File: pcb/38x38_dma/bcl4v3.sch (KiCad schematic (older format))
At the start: 23 parts, among them J1 Conn_01x04, J10 Conn_01x04, J2 Conn_01x04, J3 Conn_01x04, J4 Conn_01x04, J5 Conn_01x04, J6 Conn_01x04, J7 Conn_01x04, J8 Conn_01x04, J9 USB_MICRO-B_FEMALE-SMT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

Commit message: Board update
fully routed PCB
indicator LED added
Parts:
- removed R2: 0R, Resistor_SMD:R_0805_2012Metric_Pad1.15x1.40mm_HandSolder, symbol Device:R_Small
- added D1: LED, LED_SMD:LED_0805_2012Metric_Castellated, symbol Device:LED
- added Q1: IRLML6402, Package_TO_SOT_SMD:SOT-23, symbol Transistor_FET:IRLML6402
- added R3: 220R, Resistor_SMD:R_0805_2012Metric_Pad1.15x1.40mm_HandSolder, symbol Device:R_Small
- added R4: R, Resistor_SMD:R_0805_2012Metric_Pad1.15x1.40mm_HandSolder, symbol Device:R
- C1, C2: footprint Capacitor_SMD:C_0805_2012Metric_Pad1.15x1.40mm_HandSolder -> Capacitor_SMD:C_0603_1608Metric_Pad1.05x0.95mm_HandSolder
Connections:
- net labels added: LED, OSC_IN, OSC_OUT
- wire segments 186 -> 192
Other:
- moved on the sheet: C1, C2, C3, C4, J10, U5, Y1

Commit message: PCB and schematics updates
- exchange STM32F070 with STM32F072 (USB w/o HSE)
- remove xtal and related components
- add boot mode jumper pads (NO)
- connect USB_VBUS with VCC via jumper (NC)
- smaller clearance for pad to solder mask
- add local library directory for externally imported
  symbols, footprints and 3D models

PCB outline
add small cut-out for USB receptacle
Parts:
- removed C1, C2: 20pF, Capacitor_SMD:C_0603_1608Metric_Pad1.05x0.95mm_HandSolder, symbol Device:C_Small
- removed J9: USB_MICRO-B_FEMALE-SMT, Connectors:USB-B-MICRO-SMD, symbol SparkFun-Connectors:USB_MICRO-B_FEMALE-SMT
- removed R3: 220R, Resistor_SMD:R_0805_2012Metric_Pad1.15x1.40mm_HandSolder, symbol Device:R_Small
- removed U1: STM32F070CBTx, Package_QFP:LQFP-48_7x7mm_P0.5mm, symbol MCU_ST_STM32F0:STM32F070CBTx
- removed Y1: 8Mhz, Crystal:Crystal_SMD_Abracon_ABM7-2Pin_6.0x3.5mm, symbol Device:Crystal
- added BOOT0: Jumper_2_Open, Jumpers:SMT-JUMPER_2_NO_SILK, symbol Jumper:Jumper_2_Open
- added C5, C6, C7, C8: C_Small, Capacitor_SMD:C_0805_2012Metric_Pad1.15x1.40mm_HandSolder, symbol Device:C_Small
- added J9: 10118194-0001LF, digikey-footprints:USB_Micro_B_Female_10118194-0001LF, symbol dk_USB-DVI-HDMI-Connectors:10118194-0001LF
- added JP1: Jumper, Jumpers:SMT-JUMPER_2_NC_TRACE_NO-SILK, symbol Device:Jumper
- added R2: 1k, Resistor_SMD:R_0805_2012Metric_Pad1.15x1.40mm_HandSolder, symbol Device:R_Small
- added U1: STM32F072CBTx, Package_QFP:LQFP-48_7x7mm_P0.5mm, symbol MCU_ST_STM32F0:STM32F072CBTx
- C3, C4: value C_Small -> 4.7u
- DS1: value TC15-11SRWA -> LDM-1588BS
- J10: footprint Connector_PinHeader_2.54mm:PinHeader_1x04_P2.54mm_Horizontal -> Connector_PinHeader_2.54mm:PinHeader_1x04_P2.54mm_Vertical
- R1: value R -> 1k
- R4: value R -> 680R
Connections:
- net labels added: BOOT0
- net labels removed: OSC_IN, OSC_OUT
- wire segments 192 -> 195
- no-connect marks 2 -> 19
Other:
- moved on the sheet: C3, C4, D1, DS1, J1, J10, J2, J3, J4, J5, J6, J7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

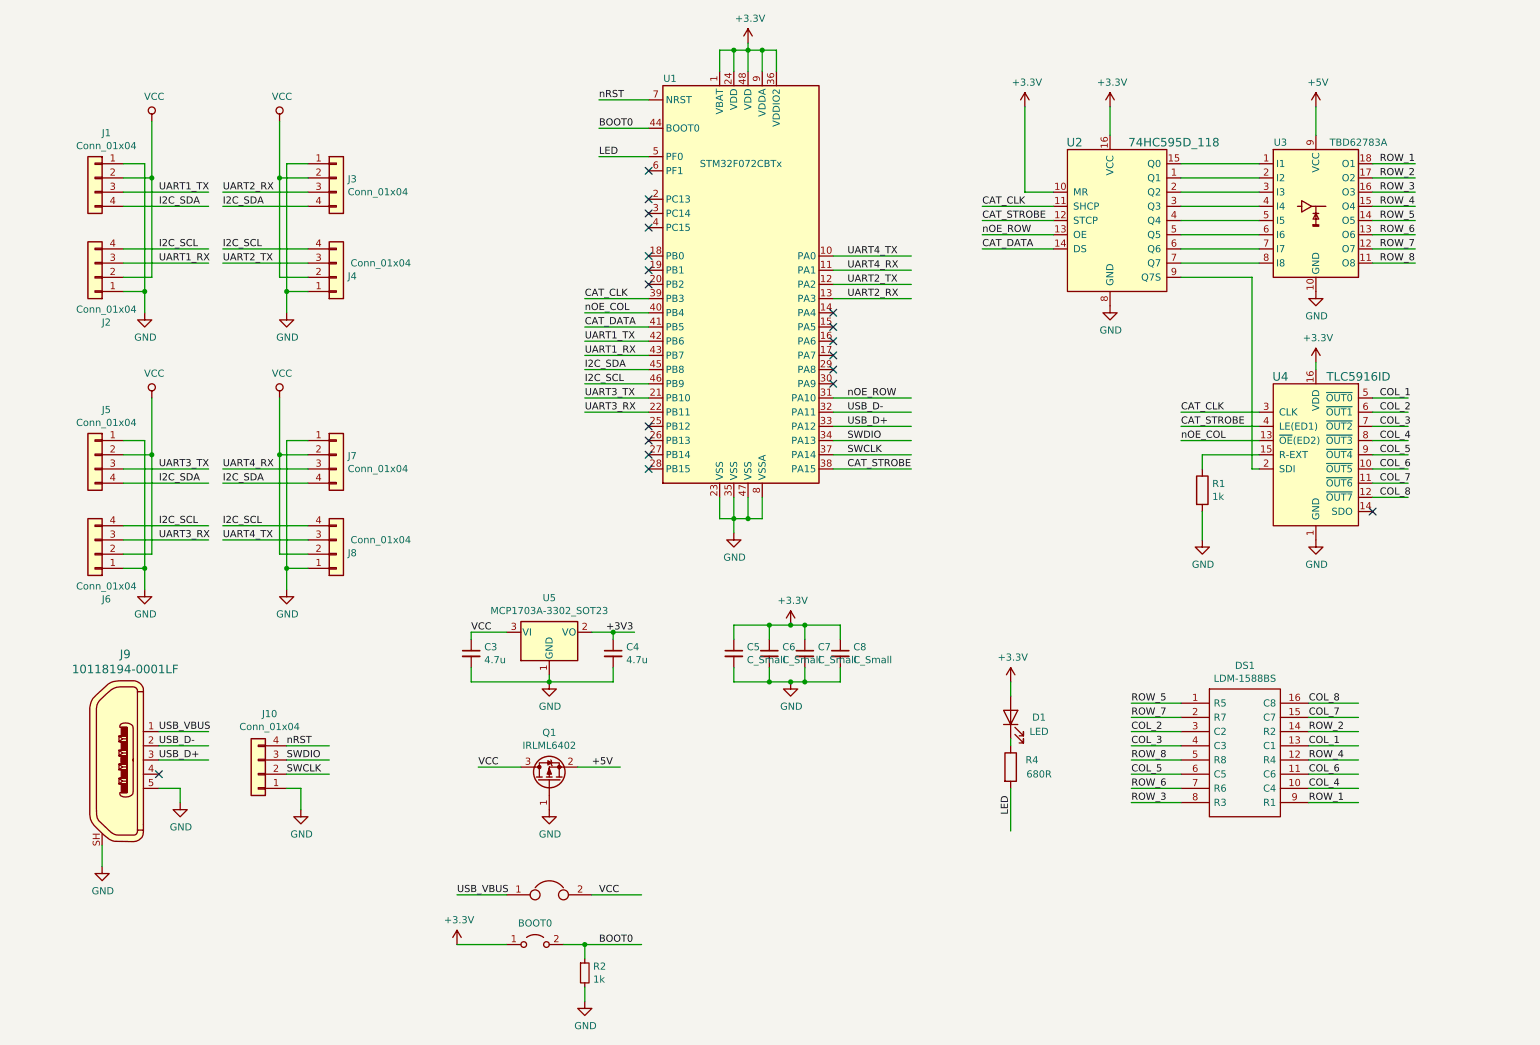
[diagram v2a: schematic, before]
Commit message: PCB and schematics cleanup
resize PCB to exactly 38x38mm, center the LED matrix
add OSHW logo to silk screen, add copyright information
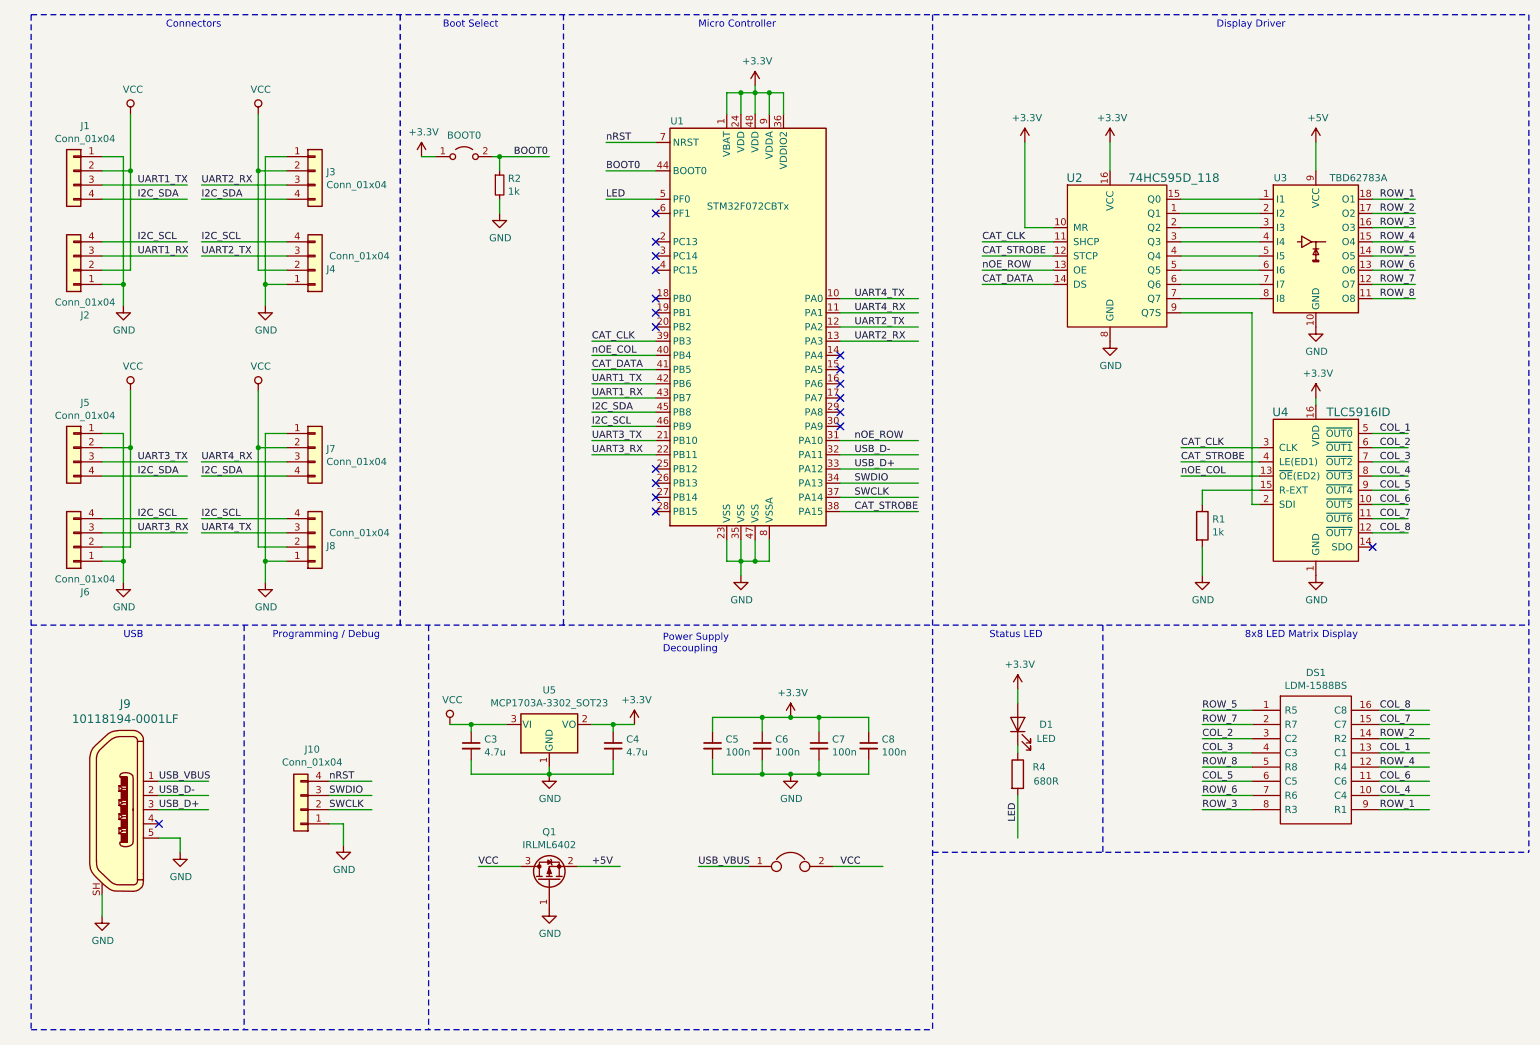
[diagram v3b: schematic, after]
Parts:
- C5, C6, C7, C8: value C_Small -> 100n
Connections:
- net labels removed: +3V3
- wire segments 195 -> 196
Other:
- note added: "8x8 LED Matrix Display"
- note added: "Boot Select"
- note added: "Connectors"
- note added: "Display Driver"
- note added: "Micro Controller"
- note added: "Power Supply\nDecoupling"
- note added: "Programming / Debug"
- note added: "Status LED"
- note added: "USB"
- moved on the sheet: BOOT0, C3, C4, C5, C6, C7, C8, D1, DS1, J1, J10, J2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

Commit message: Fix reverse voltage protection, cleanups
- power from USB doesn't need to go through protection FET
- power to 3.3V LDO _must_ got through protection FET
- add OSHW logo also to schematics so that it doesn't vanish if you
  sync PCB and schematics
- modify copyright info a bit
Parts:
- added LOGO1: OSHW-LOGOM, OSHW-LOGO-M, symbol SparkFun-Aesthetics:OSHW-LOGOM
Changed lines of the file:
@@
 	1050 4250 1650 4250
-$Comp
-L power:VCC #PWR0117
-U 1 1 5BF09410
-P 1250 1300
-F 0 "#PWR0117" H 1250 1150 50  0001 C CNN
-F 1 "VCC" H 1267 1473 50  0000 C CNN
-F 2 "" H 1250 1300 50  0001 C CNN
-F 3 "" H 1250 1300 50  0001 C CNN
-	1    1250 1300
-	1    0    0    -1
-$EndComp
-$Comp
-L power:VCC #PWR0118
-U 1 1 5BF09465
-P 2150 1300
-F 0 "#PWR0118" H 2150 1150 50  0001 C CNN
-F 1 "VCC" H 2167 1473 50  0000 C CNN
-F 2 "" H 2150 1300 50  0001 C CNN
-F 3 "" H 2150 1300 50  0001 C CNN
-	1    2150 1300
-	1    0    0    -1
-$EndComp
-$Comp
-L power:VCC #PWR0119
-U 1 1 5BF094BA
-P 1250 3250
-F 0 "#PWR0119" H 1250 3100 50  0001 C CNN
-F 1 "VCC" H 1267 3423 50  0000 C CNN
-F 2 "" H 1250 3250 50  0001 C CNN
-F 3 "" H 1250 3250 50  0001 C CNN
-	1    1250 3250
-	1    0    0    -1
-$EndComp
-$Comp
-L power:VCC #PWR0120
-U 1 1 5BF0950F
-P 2150 3250
-F 0 "#PWR0120" H 2150 3100 50  0001 C CNN
-F 1 "VCC" H 2167 3423 50  0000 C CNN
-F 2 "" H 2150 3250 50  0001 C CNN
-F 3 "" H 2150 3250 50  0001 C CNN
-	1    2150 3250
-	1    0    0    -1
-$EndComp
 $Comp
 L Regulator_Linear:MCP1703A-3302_SOT23 U5
@@
 USB_VBUS
 Text Label 6250 6600 0    50   ~ 0
-VCC
++5V
 $Comp
 L Device:C_Small C5
@@
 NoConn ~ 4950 4100
 $Comp
-L power:+3.3V #PWR?
+L power:+3.3V #PWR0128
 U 1 1 5BF60507
 P 4800 5600
-F 0 "#PWR?" H 4800 5450 50  0001 C CNN
+F 0 "#PWR0128" H 4800 5450 50  0001 C CNN
 F 1 "+3.3V" H 4815 5773 50  0000 C CNN
 F 2 "" H 4800 5600 50  0001 C CNN
 F 3 "" H 4800 5600 50  0001 C CNN
 	1    4800 5600
-	1    0    0    -1
-$EndComp
-$Comp
-L power:VCC #PWR?
-U 1 1 5BF60582
-P 3500 5600
-F 0 "#PWR?" H 3500 5450 50  0001 C CNN
-F 1 "VCC" H 3517 5773 50  0000 C CNN
-F 2 "" H 3500 5600 50  0001 C CNN
-F 3 "" H 3500 5600 50  0001 C CNN
-	1    3500 5600
 	1    0    0    -1
 $EndComp
@@
 Text Notes 2250 5000 0    50   ~ 0
 Programming / Debug
+$Comp
+L power:+5V #PWR0129
+U 1 1 5BFEB2FC
+P 3500 5600
+F 0 "#PWR0129" H 3500 5450 50  0001 C CNN
+F 1 "+5V" H 3515 5773 50  0000 C CNN
+F 2 "" H 3500 5600 50  0001 C CNN
+F 3 "" H 3500 5600 50  0001 C CNN
+	1    3500 5600
+	1    0    0    -1
+$EndComp
+$Comp
+L power:VCC #PWR0119
+U 1 1 5BF094BA
+P 1250 3250
+F 0 "#PWR0119" H 1250 3100 50  0001 C CNN
+F 1 "VCC" H 1267 3423 50  0000 C CNN
+F 2 "" H 1250 3250 50  0001 C CNN
+F 3 "" H 1250 3250 50  0001 C CNN
+	1    1250 3250
+	1    0    0    -1
+$EndComp
+$Comp
+L power:VCC #PWR0120
+U 1 1 5BF0950F
+P 2150 3250
+F 0 "#PWR0120" H 2150 3100 50  0001 C CNN
+F 1 "VCC" H 2167 3423 50  0000 C CNN
+F 2 "" H 2150 3250 50  0001 C CNN
+F 3 "" H 2150 3250 50  0001 C CNN
+	1    2150 3250
+	1    0    0    -1
+$EndComp
+$Comp
+L power:VCC #PWR0118
+U 1 1 5BF09465
+P 2150 1300
+F 0 "#PWR0118" H 2150 1150 50  0001 C CNN
+F 1 "VCC" H 2167 1473 50  0000 C CNN
+F 2 "" H 2150 1300 50  0001 C CNN
+F 3 "" H 2150 1300 50  0001 C CNN
+	1    2150 1300
+	1    0    0    -1
+$EndComp
+$Comp
+L power:VCC #PWR0117
+U 1 1 5BF09410
+P 1250 1300
+F 0 "#PWR0117" H 1250 1150 50  0001 C CNN
+F 1 "VCC" H 1267 1473 50  0000 C CNN
+F 2 "" H 1250 1300 50  0001 C CNN
+F 3 "" H 1250 1300 50  0001 C CNN
+	1    1250 1300
+	1    0    0    -1
+$EndComp
+$Comp
+L SparkFun-Aesthetics:OSHW-LOGOM LOGO1
+U 1 1 5BFECBD9
+P 3750 4450
+F 0 "LOGO1" H 3750 4700 45  0001 C CNN
+F 1 "OSHW-LOGOM" H 3750 4050 45  0001 C CNN
+F 2 "OSHW-LOGO-M" H 3750 4750 20  0001 C CNN
+F 3 "" H 3750 4450 50  0001 C CNN
+F 4 "XXX-00000" H 4228 4385 60  0001 L CNN "Field4"
+	1    3750 4450
+	1    0    0    -1
+$EndComp
 $EndSCHEMATC

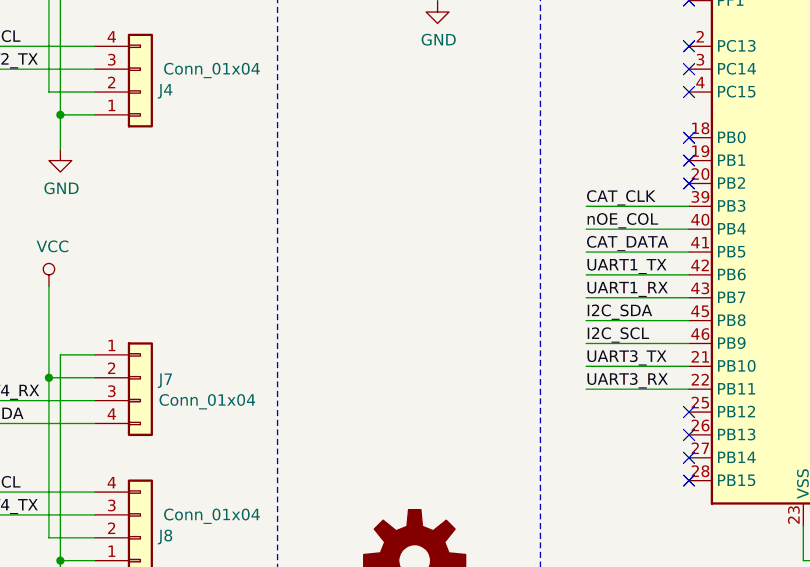
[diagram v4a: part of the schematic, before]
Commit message: Add test points, small routing changes
- add test points for SPI bus
- add net classes for VCC and LED networks
- small routing changes
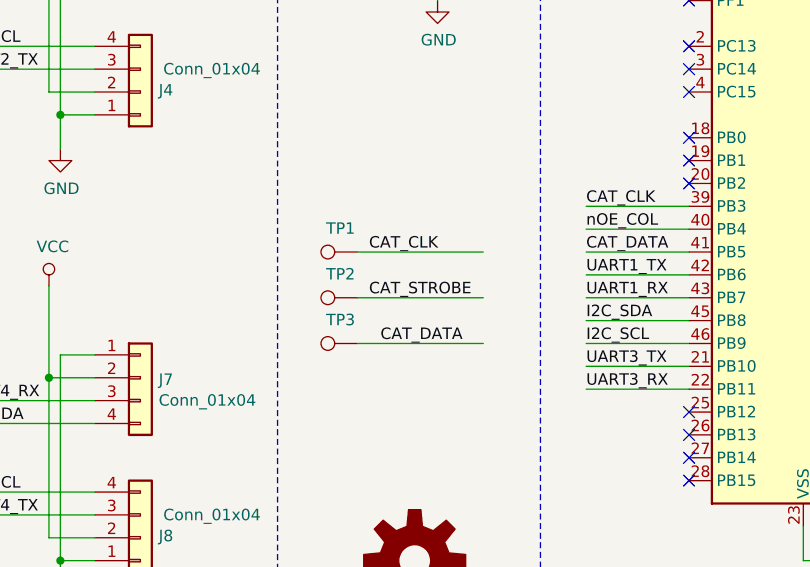
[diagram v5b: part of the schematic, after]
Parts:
- added TP1, TP2, TP3: TestPoint, TestPoint:TestPoint_THTPad_1.0x1.0mm_Drill0.5mm, symbol Connector:TestPoint
- LOGO1: footprint OSHW-LOGO-M -> Aesthetics:OSHW-LOGO-M
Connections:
- wire segments 196 -> 199
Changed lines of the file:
@@
 F 0 "LOGO1" H 3750 4700 45  0001 C CNN
 F 1 "OSHW-LOGOM" H 3750 4050 45  0001 C CNN
-F 2 "OSHW-LOGO-M" H 3750 4750 20  0001 C CNN
+F 2 "Aesthetics:OSHW-LOGO-M" H 3750 4750 20  0001 C CNN
 F 3 "" H 3750 4450 50  0001 C CNN
 F 4 "XXX-00000" H 4228 4385 60  0001 L CNN "Field4"
@@
 	1    0    0    -1
 $EndComp
+$Comp
+L Connector:TestPoint TP1
+U 1 1 5C01787F
+P 3500 3100
+F 0 "TP1" V 3603 3174 50  0000 C CNN
+F 1 "TestPoint" V 3604 3174 50  0001 C CNN
+F 2 "TestPoint:TestPoint_THTPad_1.0x1.0mm_Drill0.5mm" H 3700 3100 50  0001 C CNN
+F 3 "~" H 3700 3100 50  0001 C CNN
+	1    3500 3100
+	0    -1   -1   0
+$EndComp
+$Comp
+L Connector:TestPoint TP2
+U 1 1 5C03F55A
+P 3500 3300
+F 0 "TP2" V 3603 3374 50  0000 C CNN
+F 1 "TestPoint" V 3604 3374 50  0001 C CNN
+F 2 "TestPoint:TestPoint_THTPad_1.0x1.0mm_Drill0.5mm" H 3700 3300 50  0001 C CNN
+F 3 "~" H 3700 3300 50  0001 C CNN
+	1    3500 3300
+	0    -1   -1   0
+$EndComp
+$Comp
+L Connector:TestPoint TP3
+U 1 1 5C03F5B8
+P 3500 3500
+F 0 "TP3" V 3603 3574 50  0000 C CNN
+F 1 "TestPoint" V 3604 3574 50  0001 C CNN
+F 2 "TestPoint:TestPoint_THTPad_1.0x1.0mm_Drill0.5mm" H 3700 3500 50  0001 C CNN
+F 3 "~" H 3700 3500 50  0001 C CNN
+	1    3500 3500
+	0    -1   -1   0
+$EndComp
+Wire Wire Line
+	3500 3100 4050 3100
+Wire Wire Line
+	3500 3300 4050 3300
+Wire Wire Line
+	3500 3500 4050 3500
+Text Label 3550 3100 0    50   ~ 0
+CAT_CLK
+Text Label 3550 3300 0    50   ~ 0
+CAT_STROBE
+Text Label 3600 3500 0    50   ~ 0
+CAT_DATA
 $EndSCHEMATC
